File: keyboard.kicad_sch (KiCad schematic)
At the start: 104 parts

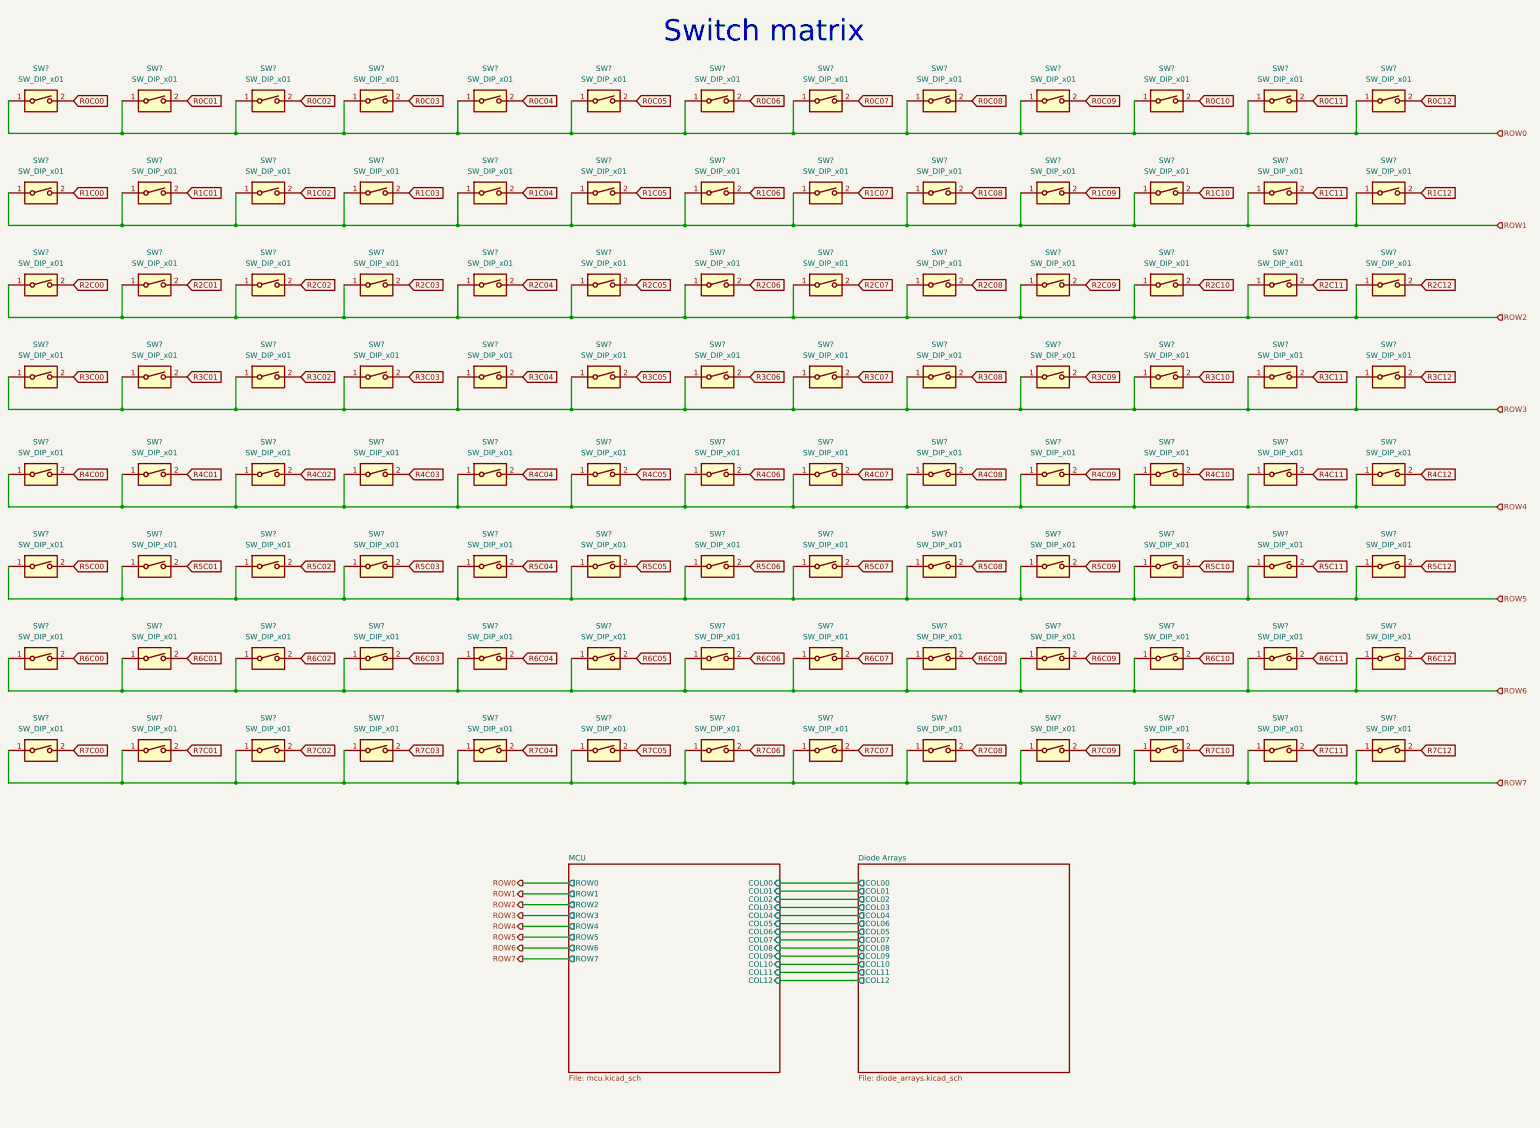
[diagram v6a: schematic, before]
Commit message: Add RGB LEDs, assign footpritns, begin placement
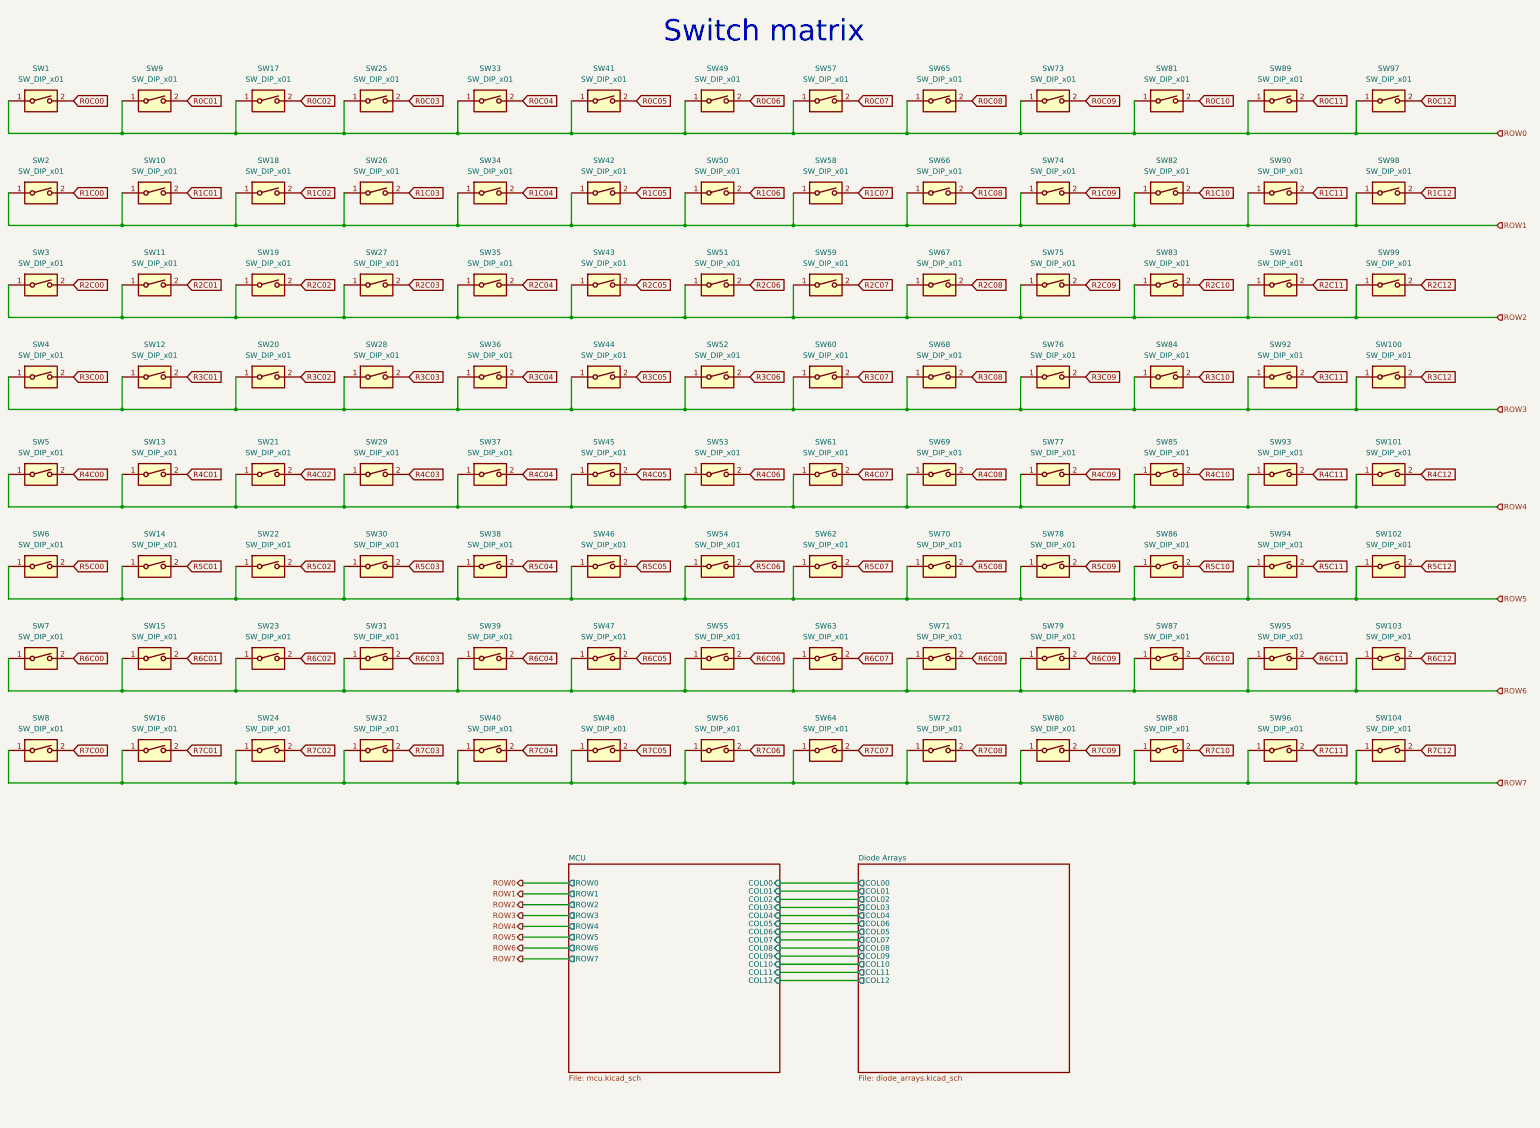
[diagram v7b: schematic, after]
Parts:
- SW1, SW10, SW100, SW101, SW102, SW103, SW104, SW11, SW12, SW13, SW14, SW15, SW16, SW17, SW18, SW19, SW2, SW20, SW21, SW22, SW23, SW24, SW25, SW26, SW27, SW28, SW29, SW3, SW30, SW31, SW32, SW33, SW34, SW35, SW36, SW37, SW38, SW39, SW4, SW40, SW41, SW42, SW43, SW44, SW45, SW46, SW47, SW48, SW49, SW5, SW50, SW51, SW52, SW53, SW54, SW55, SW56, SW57, SW58, SW59, SW6, SW60, SW61, SW62, SW63, SW64, SW65, SW66, SW67, SW68, SW69, SW7, SW70, SW71, SW72, SW73, SW74, SW75, SW76, SW77, SW78, SW79, SW8, SW80, SW81, SW82, SW83, SW84, SW85, SW86, SW87, SW88, SW89, SW9, SW90, SW91, SW92, SW93, SW94, SW95, SW96, SW97, SW98, SW99: renamed from SW?; footprint (none) -> keyswitches:Kailh_socket_MX_optional_reversible
